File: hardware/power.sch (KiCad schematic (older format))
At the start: 18 parts

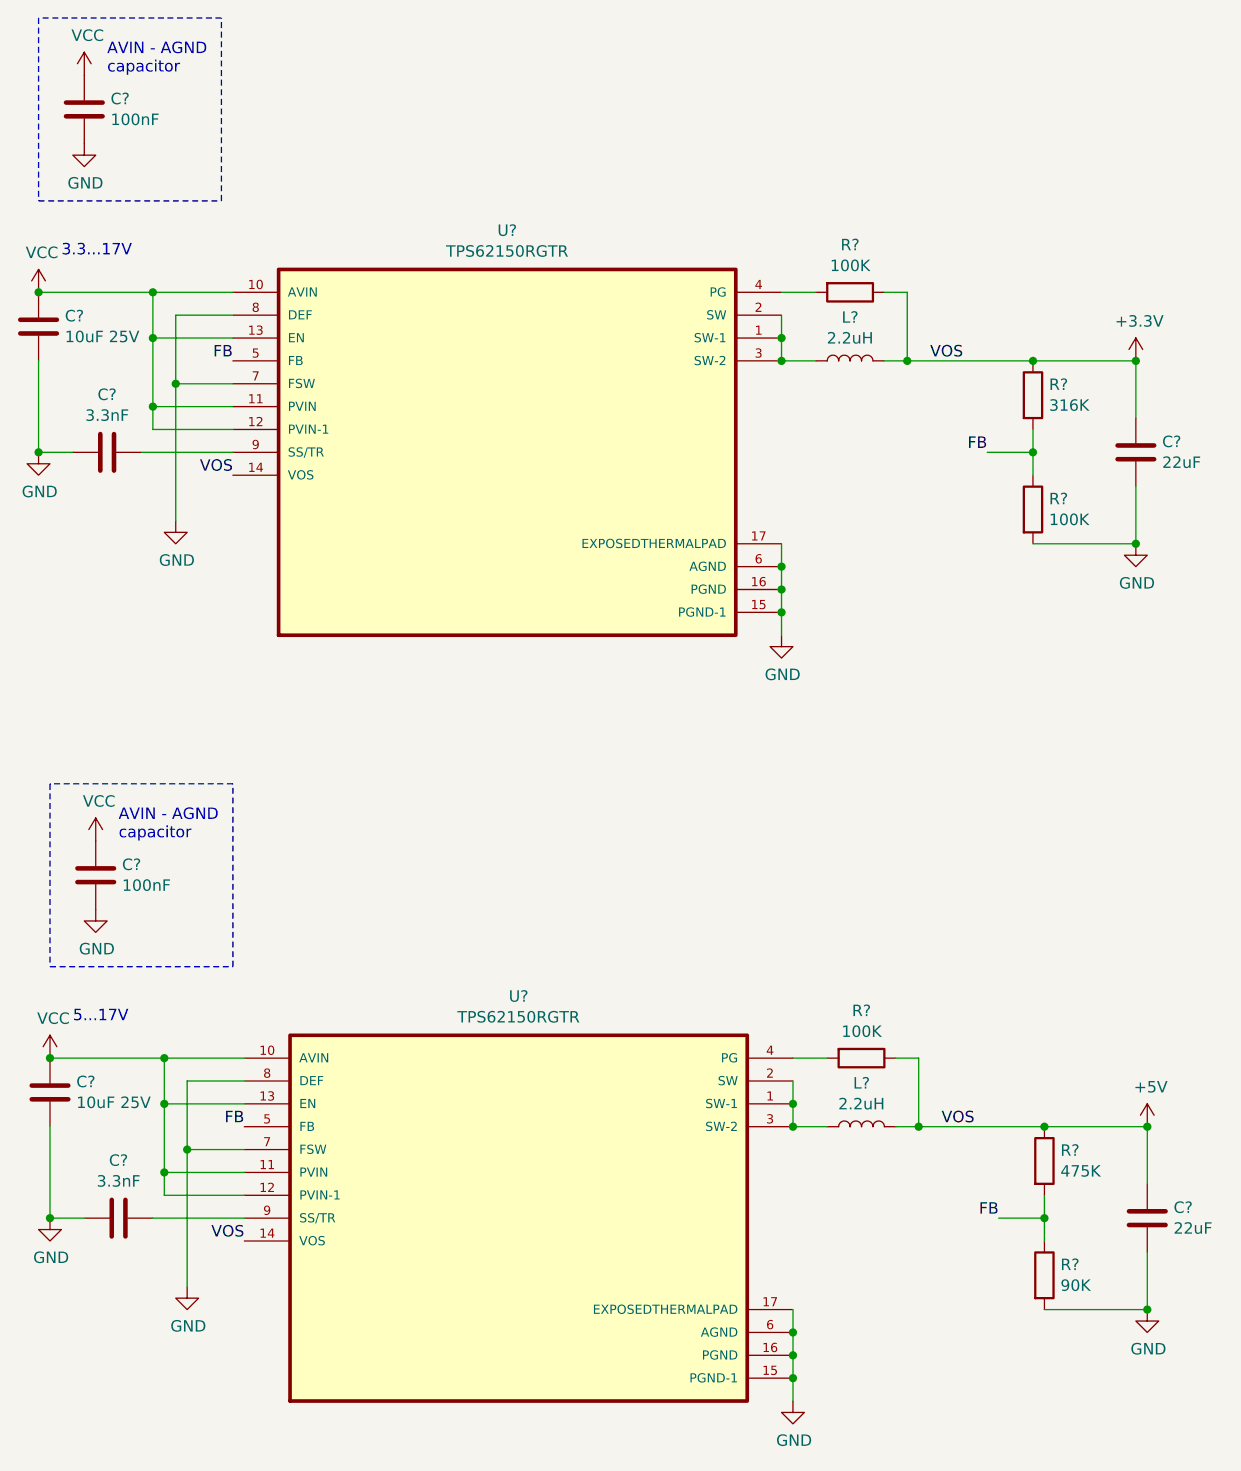
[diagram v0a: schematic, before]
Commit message: Changed atmega power to 3.3v instead of 5v Added type-c connector
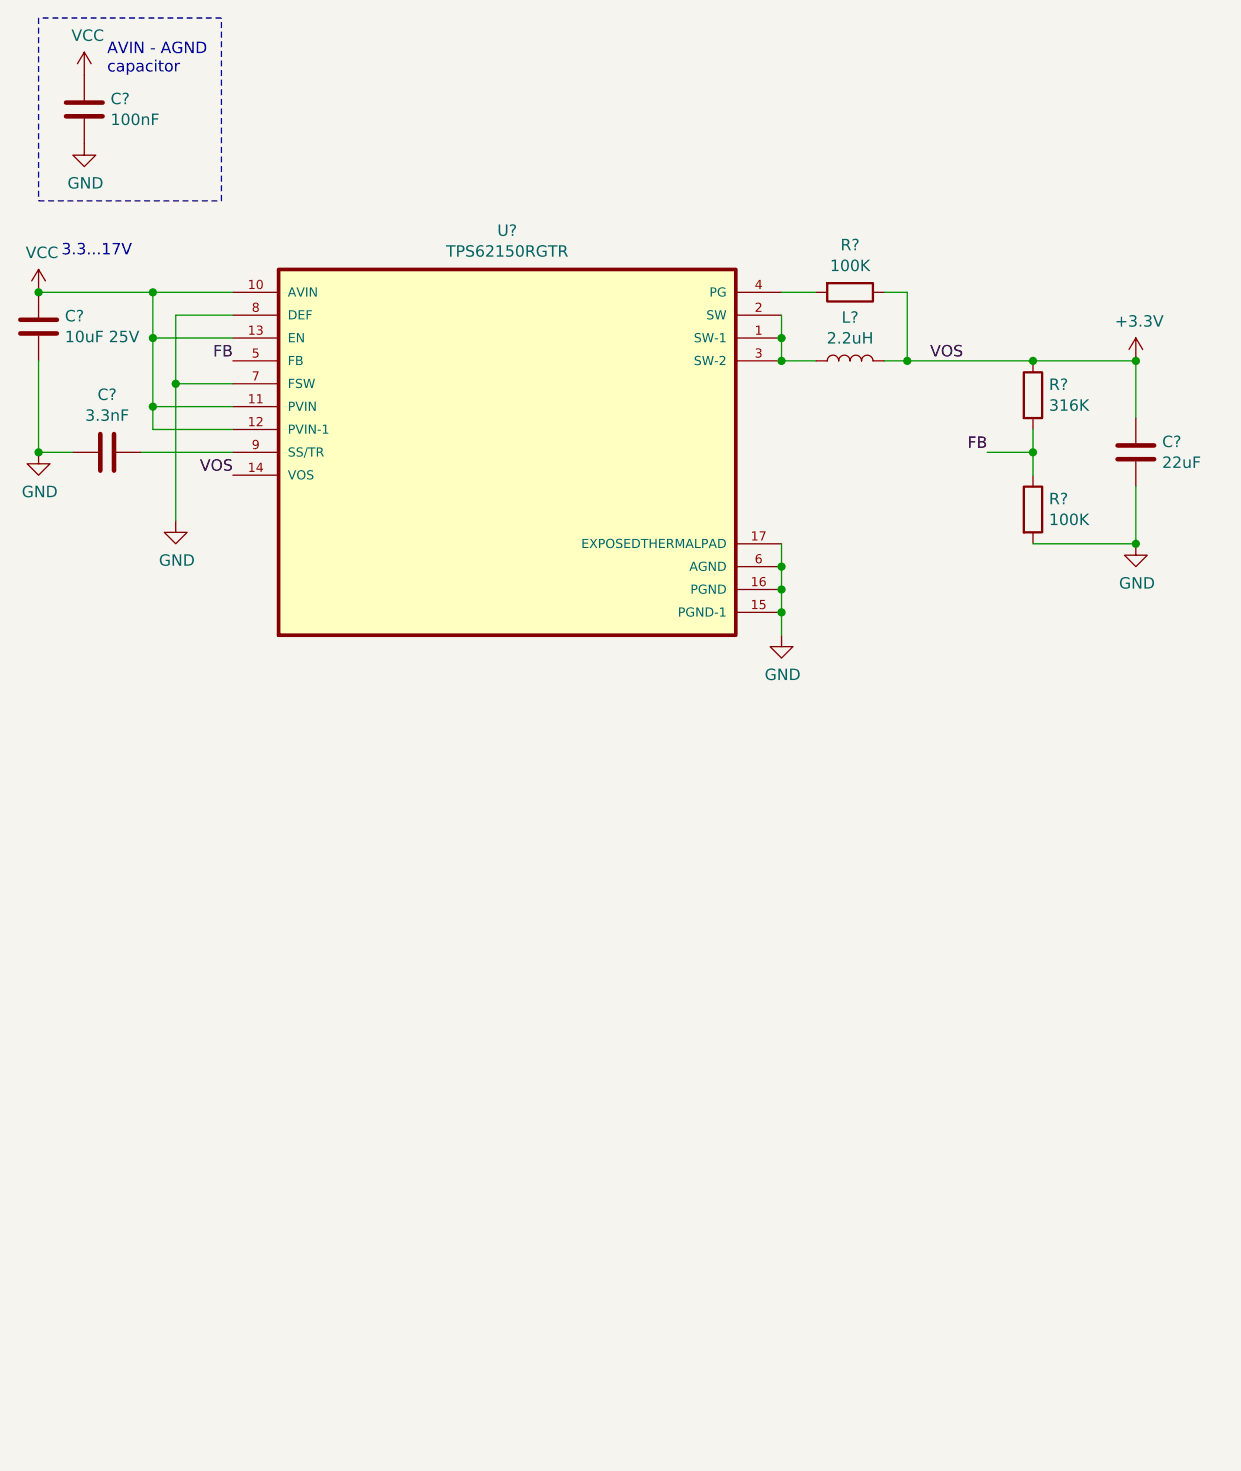
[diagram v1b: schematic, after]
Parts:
- removed C?: 10uF 25V, symbol Device:C
- removed C?: 3.3nF, symbol Device:C
- removed C?: 100nF, symbol Device:C
- removed C?: 22uF, symbol Device:C
- removed L?: 2.2uH, symbol Device:L
- removed R?: 100K, symbol Device:R
- removed R?: 475K, symbol Device:R
- removed R?: 90K, symbol Device:R
- removed U?: TPS62150RGTR, QFN50P300X300X100-17N, symbol TSP62150:TPS62150RGTR
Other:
- note removed: "5...17V"
